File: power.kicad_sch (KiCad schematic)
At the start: 51 parts, among them IC1 TPS62A02DRLR, J1 GND, Q1 STR1550, Q2 BC807, Q3 PMOS, U1 LMR33630BDDA

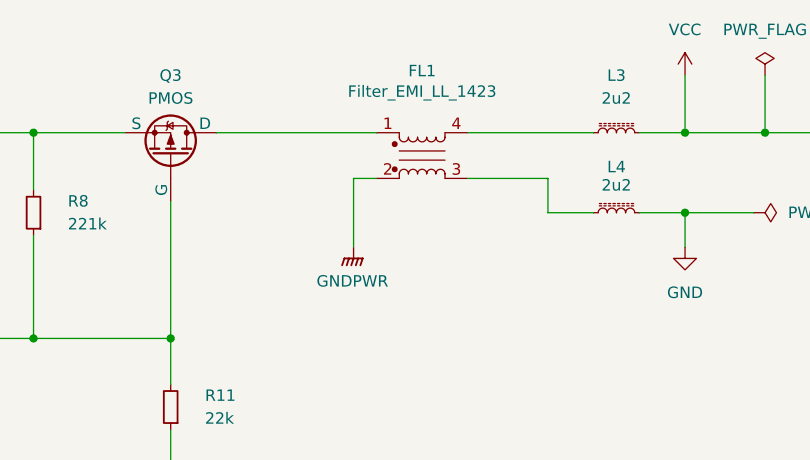
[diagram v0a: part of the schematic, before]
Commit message: power: removed FL1
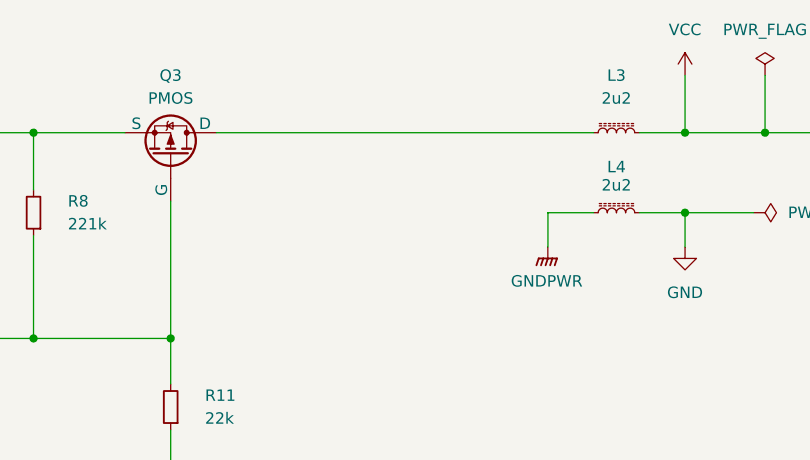
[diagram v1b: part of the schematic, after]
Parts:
- removed FL1: Filter_EMI_LL_1423, symbol Device:Filter_EMI_LL_1423
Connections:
- net GNDPWR: now also L4.1
- net at L3.1: now also Q3.1 (D)
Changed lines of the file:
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@@
 	(wire
 		(pts
-			(xy 264.16 67.31) (xy 273.05 67.31)
+			(xy 273.05 71.12) (xy 278.13 71.12)
 		)
 		(stroke
@@
 	(wire
 		(pts
-			(xy 236.22 62.23) (xy 254 62.23)
-		)
-		(stroke
-			(width 0)
-			(type default)
-		)
-	)
-	(wire
-		(pts
 			(xy 223.52 135.89) (xy 229.87 135.89)
 		)
@@
 	(wire
 		(pts
-			(xy 254 67.31) (xy 251.46 67.31)
-		)
-		(stroke
-			(width 0)
-			(type default)
-		)
-	)
-	(wire
-		(pts
 			(xy 229.87 143.51) (xy 229.87 144.78)
 		)
@@
 	(wire
 		(pts
-			(xy 251.46 67.31) (xy 251.46 74.93)
+			(xy 273.05 71.12) (xy 273.05 74.93)
 		)
 		(stroke
@@
 	(wire
 		(pts
-			(xy 264.16 62.23) (xy 278.13 62.23)
+			(xy 236.22 62.23) (xy 278.13 62.23)
 		)
 		(stroke
@@
 	(wire
 		(pts
-			(xy 273.05 67.31) (xy 273.05 71.12)
-		)
-		(stroke
-			(width 0)
-			(type default)
-		)
-	)
-	(wire
-		(pts
 			(xy 284.48 135.89) (xy 284.48 143.51)
 		)
@@
 	(wire
 		(pts
-			(xy 273.05 71.12) (xy 278.13 71.12)
-		)
-		(stroke
-			(width 0)
-			(type default)
-		)
-	)
-	(wire
-		(pts
 			(xy 182.88 195.58) (xy 180.34 195.58)
 		)
@@
 	(symbol
 		(lib_id "power:GNDPWR")
-		(at 251.46 74.93 0)
+		(at 273.05 74.93 0)
 		(unit 1)
 		(exclude_from_sim no)
@@
 		(fields_autoplaced yes)
 		(property "Reference" "#PWR018"
-			(at 251.46 80.01 0)
+			(at 273.05 80.01 0)
 			(effects
 				(font
@@
 		)
 		(property "Value" "GNDPWR"
-			(at 251.333 78.74 0)
+			(at 272.923 78.74 0)
 			(effects
 				(font
@@
 		)
 		(property "Footprint" ""
-			(at 251.46 76.2 0)
+			(at 273.05 76.2 0)
 			(effects
 				(font
@@
 		)
 		(property "Datasheet" ""
-			(at 251.46 76.2 0)
+			(at 273.05 76.2 0)
 			(effects
 				(font
@@
 		)
 		(property "Description" "Power symbol creates a global label with name \"GNDPWR\" , global ground"
-			(at 251.46 74.93 0)
+			(at 273.05 74.93 0)
 			(effects
 				(font
@@
 					(unit 1)
 				)
-			)
-		)
-	)
-	(symbol
-		(lib_id "Device:Filter_EMI_LL_1423")
-		(at 259.08 64.77 0)
-		(mirror x)
-		(unit 1)
-		(exclude_from_sim no)
-		(in_bom yes)
-		(on_board yes)
-		(dnp no)
-		(property "Reference" "FL1"
-			(at 259.08 55.372 0)
-			(effects
-				(font
-					(size 1.27 1.27)
-				)
-			)
-		)
-		(property "Value" "Filter_EMI_LL_1423"
-			(at 259.08 57.658 0)
-			(effects
-				(font
-					(size 1.27 1.27)
-				)
-			)
-		)
-		(property "Footprint" ""
-			(at 259.08 58.42 0)
-			(effects
-				(font
-					(size 1.27 1.27)
-				)
-				(hide yes)
-			)
-		)
-		(property "Datasheet" "~"
-			(at 259.08 65.786 90)
-			(effects
-				(font
-					(size 1.27 1.27)
-				)
-				(hide yes)
-			)
-		)
-		(property "Description" "EMI 2-inductor filter, pin-connections 1-4 and 2-3"
-			(at 259.08 64.77 0)
-			(effects
-				(font
-					(size 1.27 1.27)
-				)
-				(hide yes)
-			)
-		)
-		(pin "2"
-		)
-		(pin "1"
-		)
-		(pin "3"
-		)
-		(pin "4"
-		)
-		(instances
-			(project "haldex_controller"
-				(path "/f9b060b2-b7a5-478e-9a0d-346ba4acb11f/86767b70-18e0-4c81-b43a-e2960c44587b"
-					(reference "FL1")
-					(unit 1)
-				)

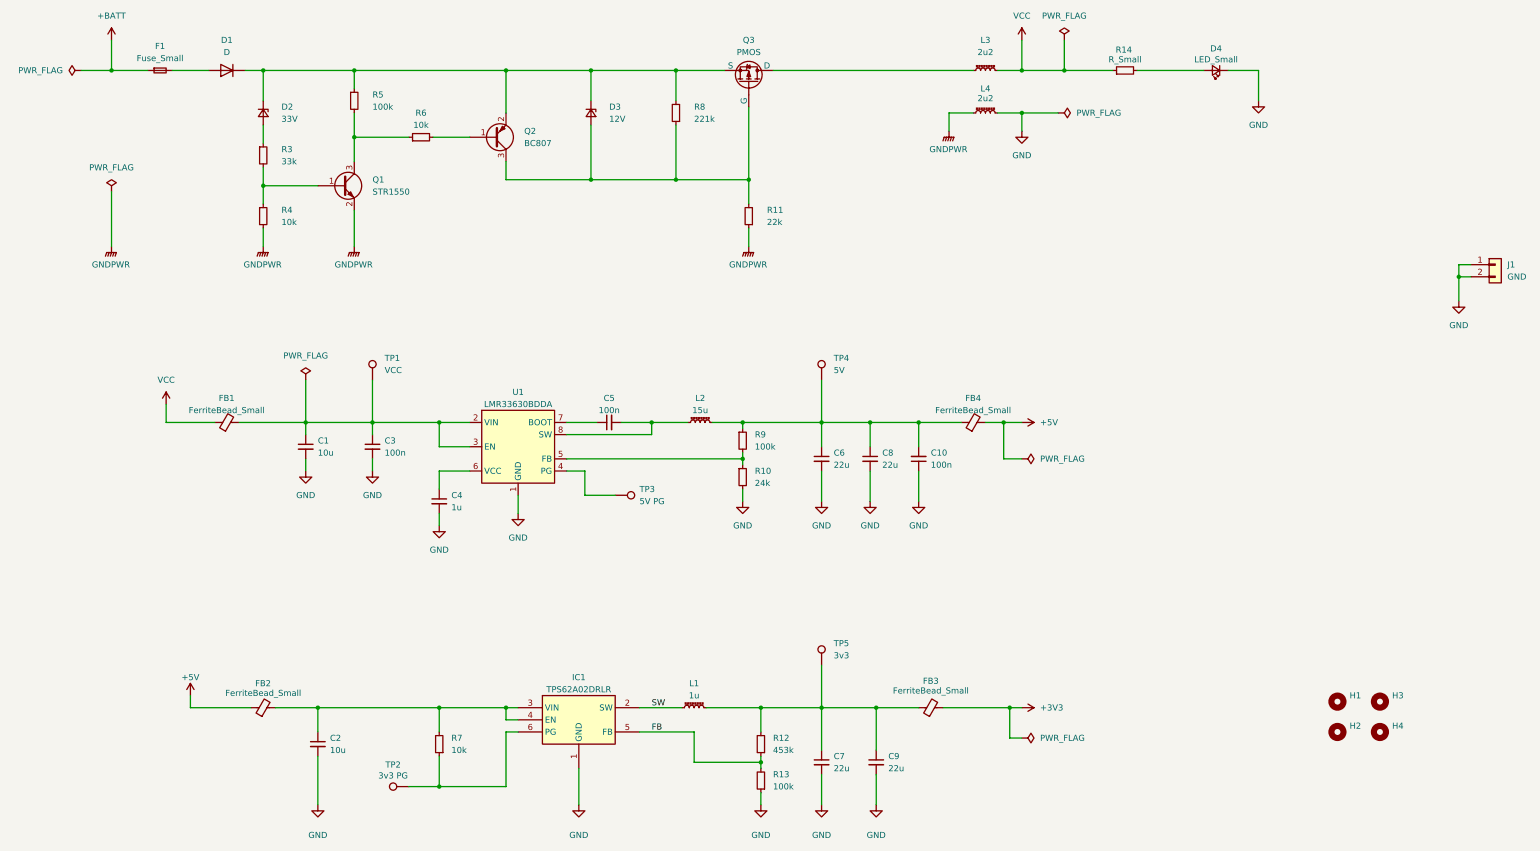
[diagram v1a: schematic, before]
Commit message: sch: fixing component footprints
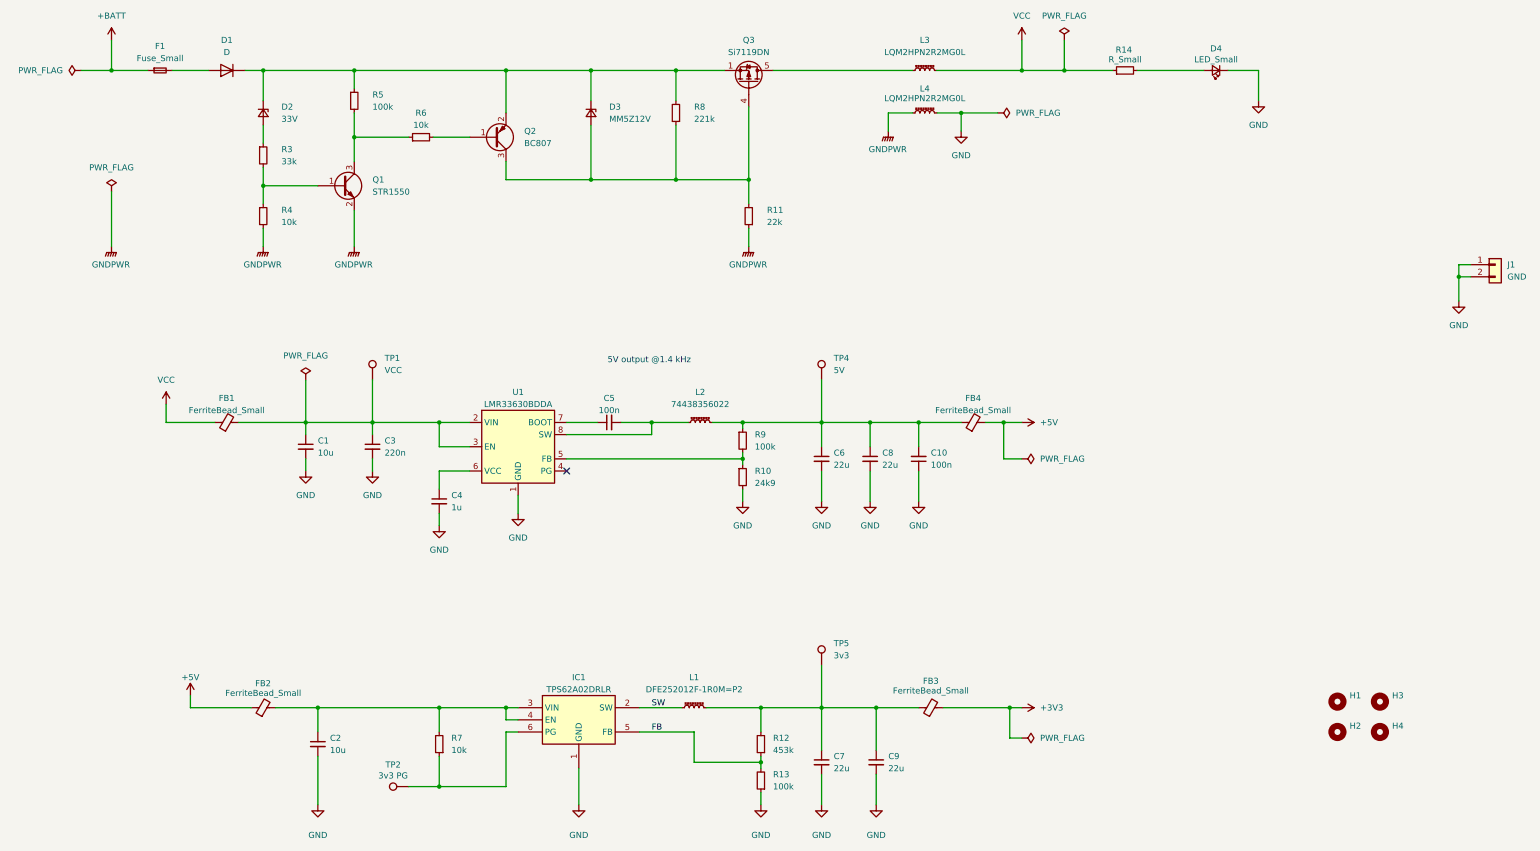
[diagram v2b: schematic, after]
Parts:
- removed Q3: PMOS, symbol Simulation_SPICE:PMOS
- removed TP3: 5V PG, TestPoint:TestPoint_Pad_D1.0mm, symbol Connector:TestPoint
- added Q3: Si7119DN, Package_SO:Vishay_PowerPAK_1212-8_Single, symbol Transistor_FET:SiSS27DN
- C3: value 100n -> 220n
- D3: value 12V -> MM5Z12V; footprint Diode_SMD:D_SOD-123 -> Diode_SMD:D_SOD-523
- FB1, FB2, FB3, FB4: footprint (none) -> Inductor_SMD:L_0805_2012Metric_Pad1.05x1.20mm_HandSolder
- H1, H2, H3, H4: footprint (none) -> MountingHole:MountingHole_3.2mm_M3_Pad_Via
- IC1: footprint SOTFL50P160X60-6N -> TPS62A02DRLR:SOTFL50P160X60-6N
- L1: value 1u -> DFE252012F-1R0M=P2; footprint (none) -> Inductor_SMD:L_1008_2520Metric_Pad1.43x2.20mm_HandSolder
- L2: value 15u -> 74438356022; footprint (none) -> Inductor_SMD:L_Wuerth_MAPI-4020
- L3, L4: value 2u2 -> LQM2HPN2R2MG0L; footprint (none) -> Inductor_SMD:L_1008_2520Metric_Pad1.43x2.20mm_HandSolder
- Q1: footprint (none) -> Package_TO_SOT_SMD:TSOT-23
- R10: value 24k -> 24k9
- TP1, TP4, TP5: footprint (none) -> TestPoint:TestPoint_Pad_D1.5mm
- U1: footprint Package_SO:Texas_HSOP-8-1EP_3.9x4.9mm_P1.27mm -> Package_SO:Texas_HSOP-8-1EP_3.9x4.9mm_P1.27mm_ThermalVias
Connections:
- net at D1.1 (K), D2.1 (K), D3.1 (K)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: now also Q3.1 (S), Q3.2 (S), Q3.3 (S)
- net at L3.1: now also Q3.5 (D)
- net at D3.2 (A), Q2.3 (C), R11.2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: now also Q3.4 (G)
- no-connect marks 0 -> 1
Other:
- note added: "5V output @1.4 kHz"
- moved on the sheet: L3, L4

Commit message: sch: fix association with mounting holes and sw1/sw2
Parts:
- H1, H2, H3, H4: footprint MountingHole:MountingHole_3.2mm_M3_Pad_Via -> MountingHole:MountingHole_3.2mm_M3
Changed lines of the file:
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@@
 			)
 		)
-		(property "Footprint" "MountingHole:MountingHole_3.2mm_M3_Pad_Via"
+		(property "Footprint" "MountingHole:MountingHole_3.2mm_M3"
 			(at 363.22 200.66 0)
 			(effects
@@
 			)
 		)
-		(property "Footprint" "MountingHole:MountingHole_3.2mm_M3_Pad_Via"
+		(property "Footprint" "MountingHole:MountingHole_3.2mm_M3"
 			(at 363.22 194.31 0)
 			(effects
@@
 			)
 		)
-		(property "Footprint" "MountingHole:MountingHole_3.2mm_M3_Pad_Via"
+		(property "Footprint" "MountingHole:MountingHole_3.2mm_M3"
 			(at 354.33 194.31 0)
 			(effects
@@
 			)
 		)
-		(property "Footprint" "MountingHole:MountingHole_3.2mm_M3_Pad_Via"
+		(property "Footprint" "MountingHole:MountingHole_3.2mm_M3"
 			(at 354.33 200.66 0)
 			(effects
